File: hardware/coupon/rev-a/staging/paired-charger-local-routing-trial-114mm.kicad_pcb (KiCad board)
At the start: 6 copper layers, 114 x 32.5 mm, 483 parts, among them J1 USB4505-03-0-A, J2 S2B-PH-SM4-TB, SW1 EVQP7J01P, SW2 JS202011JCQN, U1 TLC59581RTQT, U11 SN74LVC1G04DBVR, U17 SN74LVC1G11DBVR, U2 74HC4514PW,118, U23 SN74LVC1G06DBVR, U24 SN74LVC2G17DBVR, U25 SN74LVC2G17DBVR, U29 TPS70933DBVR, U3 ESP32-S3-WROOM-1U-N16R8, U31 TUSB320LAIRWBR, U32 TS3USB31ERSER, U33 TPD4E05U06DQAR, U34 TPS3808G01DBVR, U35 MAX17048G+T10, U36 TPS631000DRLR, U37 TPS63020DSJT, U38 2.5V shunt, U39 TMP390A2DRLR, U40 SN74AUP1G125DBVR, U41 BQ24074RGTR, U42 SN74AUP1G125DBVR, U43 SN74AUP1G125DBVR, U44 TPS259474ARPWR, U45 TPS259474ARPWR, U46 TCA9517ADGKR, U47 TPS3823A-33DBVR, U48 SN74LVC1G04DSFR, U49 SN74LVC1G74RSER, U50 SN74LVC1G74RSER, U51 SN74LVC1G11DRYR, U52 SN74LVC1G08DSFR, U53 TLV6700DSER, U54 SN74LVC2G00DCUR, U55 SN74LVC2G08DCUR

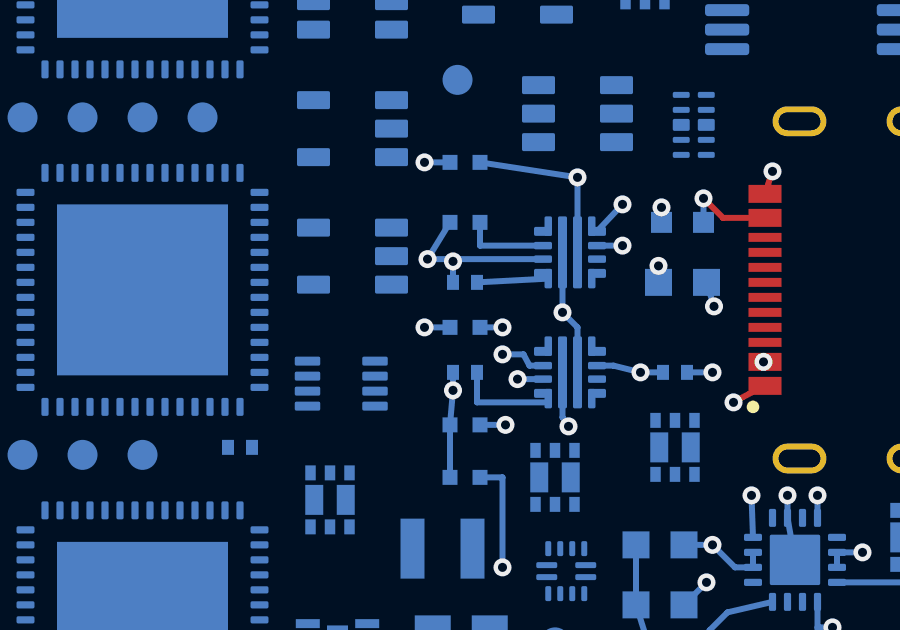
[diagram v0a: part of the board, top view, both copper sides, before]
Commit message: Route local charger permission to E1 enable
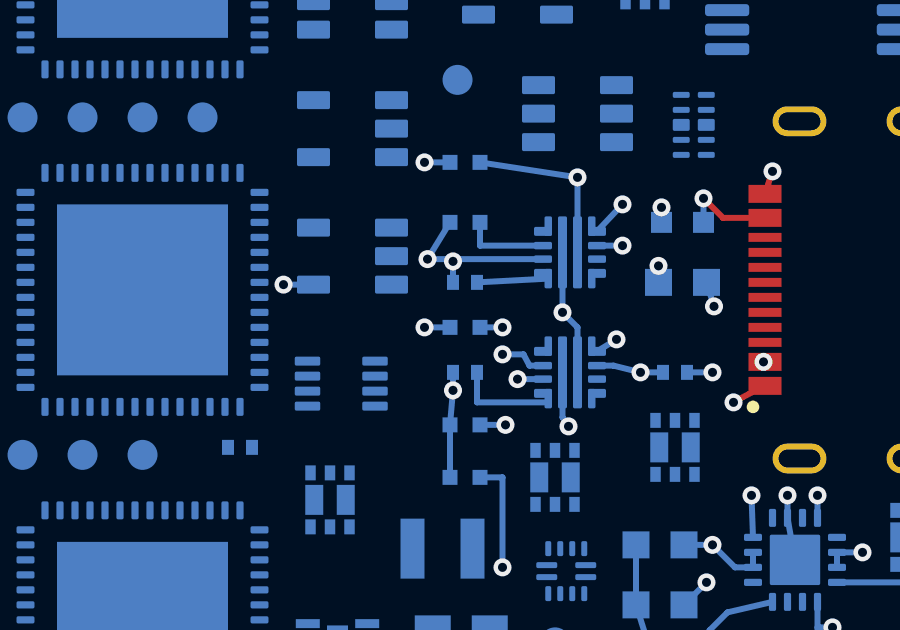
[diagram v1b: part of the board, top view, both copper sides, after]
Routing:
- net CHARGER_GATE_EN: track 0.00 -> 16.1 mm, vias 0 -> 2
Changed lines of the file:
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@@
+	)
+	(segment
+		(start 101 14.3)
+		(end 102.3 17.9)
+		(width 0.2)
+		(layer "In1.Cu")
+		(net "CHARGER_GATE_EN")
 	)
 	(segment
@@
 		(layer "B.Cu")
 		(net "GND")
+	)
+	(segment
+		(start 102.3 17.9)
+		(end 101.65 18.3)
+		(width 0.2)
+		(layer "B.Cu")
+		(net "CHARGER_GATE_EN")
 	)
 	(segment
@@
 	)
 	(segment
+		(start 91.2 16.075)
+		(end 93 14.3)
+		(width 0.2)
+		(layer "In1.Cu")
+		(net "CHARGER_GATE_EN")
+	)
+	(segment
+		(start 92.2 16.075)
+		(end 91.2 16.075)
+		(width 0.2)
+		(layer "B.Cu")
+		(net "CHARGER_GATE_EN")
+	)
+	(segment
+		(start 93 14.3)
+		(end 101 14.3)
+		(width 0.2)
+		(layer "In1.Cu")
+		(net "CHARGER_GATE_EN")
+	)
+	(segment
 		(start 95.9 12)
 		(end 100 11.5)
@@
 	)
 	(via
+		(at 102.3 17.9)
+		(size 0.6)
+		(drill 0.3)
+		(layers "F.Cu" "B.Cu")
+		(net "CHARGER_GATE_EN")
+	)
+	(via
 		(at 102.5 13.4)
 		(size 0.6)
@@
 	)
 	(via
+		(at 91.2 16.075)
+		(size 0.6)
+		(drill 0.3)
+		(layers "F.Cu" "B.Cu")
+		(net "CHARGER_GATE_EN")
+	)
+	(via

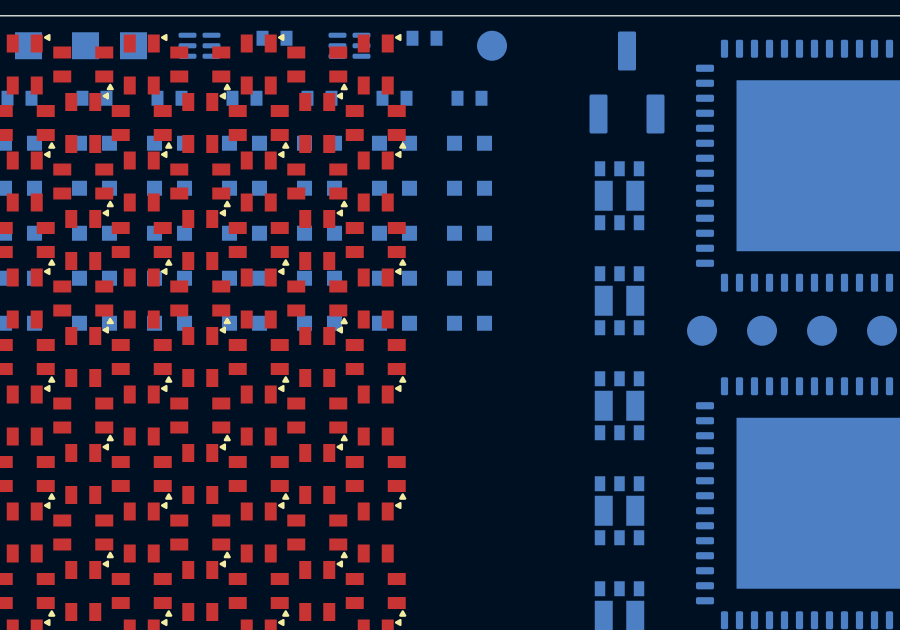
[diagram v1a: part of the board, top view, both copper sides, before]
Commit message: Connect E1 enable bias resistors on 114 mm trial
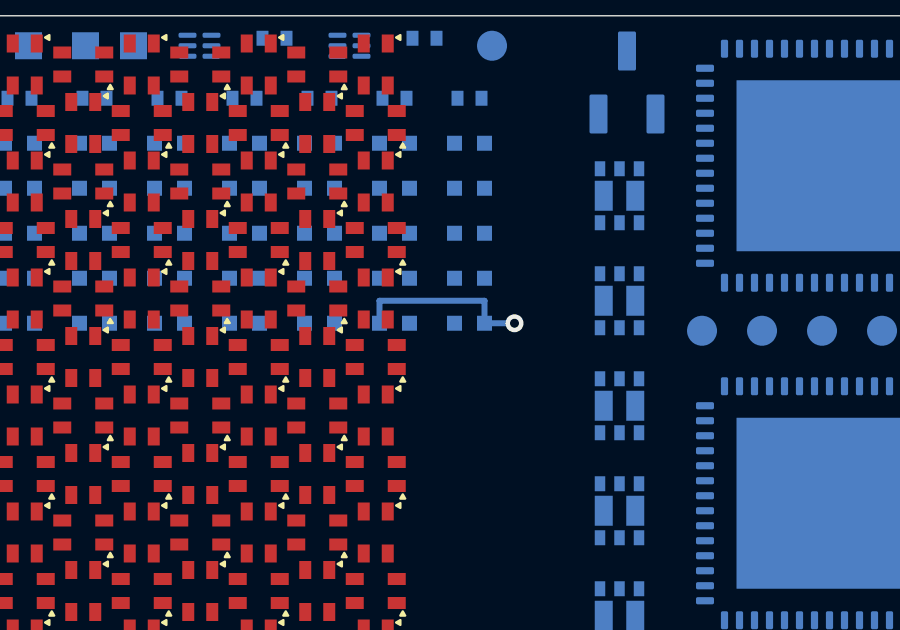
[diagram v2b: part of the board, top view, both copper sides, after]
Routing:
- net CHARGER_GATE_EN: track 16.1 -> 38.2 mm, vias 2 -> 3
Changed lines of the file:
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@@
+	)
+	(segment
+		(start 71.75 10.25)
+		(end 71.75 9.5)
+		(width 0.2)
+		(layer "B.Cu")
+		(net "CHARGER_GATE_EN")
+	)
+	(segment
+		(start 71.75 9.5)
+		(end 75.25 9.5)
+		(width 0.2)
+		(layer "B.Cu")
+		(net "CHARGER_GATE_EN")
+	)
+	(segment
+		(start 75.25 10.25)
+		(end 76.25 10.25)
+		(width 0.2)
+		(layer "B.Cu")
+		(net "CHARGER_GATE_EN")
+	)
+	(segment
+		(start 75.25 9.5)
+		(end 75.25 10.25)
+		(width 0.2)
+		(layer "B.Cu")
+		(net "CHARGER_GATE_EN")
+	)
+	(segment
+		(start 76.25 10.25)
+		(end 91.2 16.075)
+		(width 0.2)
+		(layer "In1.Cu")
+		(net "CHARGER_GATE_EN")
 	)
 	(segment
@@
 	)
 	(via
+		(at 76.25 10.25)
+		(size 0.6)
+		(drill 0.3)
+		(layers "F.Cu" "B.Cu")
+		(net "CHARGER_GATE_EN")
+	)
+	(via

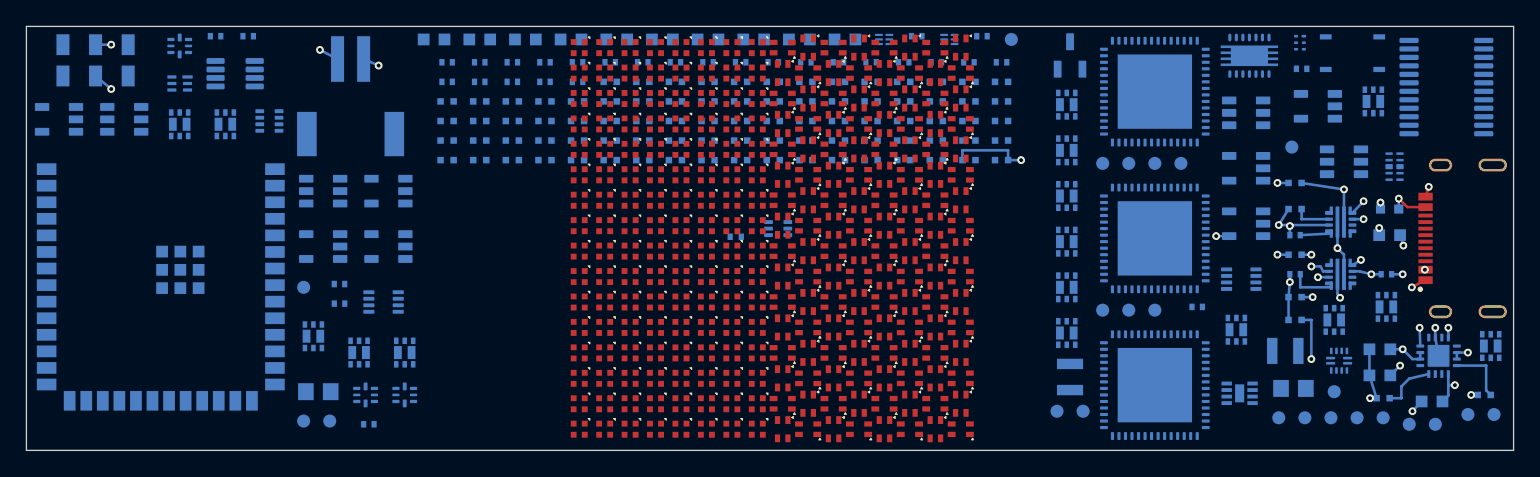
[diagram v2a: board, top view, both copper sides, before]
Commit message: Route charger inhibit node and local supervisor links on 114mm trial
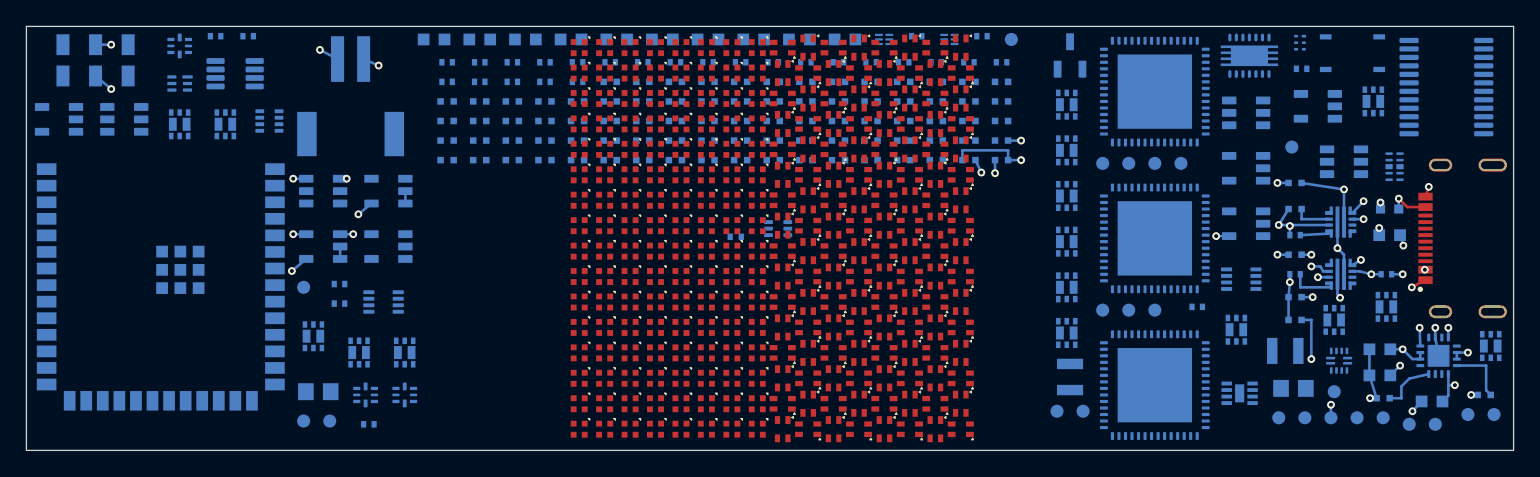
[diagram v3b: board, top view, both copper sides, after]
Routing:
- net CHARGER_GATE_EN: track 38.2 -> 126.6 mm, vias 3 -> 6
- net +3V3_USB: track 0.00 -> 12.2 mm, vias 0 -> 4
- net GND: track 182.1 -> 191.8 mm, vias 16 -> 17
- net USB_RAW_LOGIC_READY: track 0.00 -> 5.96 mm, vias 0 -> 2
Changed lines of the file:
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@@
+	)
+	(segment
+		(start 100 29)
+		(end 90 29)
+		(width 0.2)
+		(layer "In4.Cu")
+		(net "CHARGER_GATE_EN")
+	)
+	(segment
+		(start 100.001262 30.000001)
+		(end 100 29)
+		(width 0.2)
+		(layer "B.Cu")
+		(net "CHARGER_GATE_EN")
 	)
 	(segment
@@
 		(layer "B.Cu")
 		(net "CHARGER_ILIM")
+	)
+	(segment
+		(start 20.35 18.75)
+		(end 25.45 14.4)
+		(width 0.2)
+		(layer "In4.Cu")
+		(net "CHARGER_GATE_EN")
+	)
+	(segment
+		(start 20.45 11.675)
+		(end 20.45 15.925)
+		(width 0.2)
+		(layer "In2.Cu")
+		(net "+3V3_USB")
+	)
+	(segment
+		(start 21.45 11.675)
+		(end 20.45 11.675)
+		(width 0.2)
+		(layer "B.Cu")
+		(net "+3V3_USB")
+	)
+	(segment
+		(start 21.45 15.925)
+		(end 20.45 15.925)
+		(width 0.2)
+		(layer "B.Cu")
+		(net "+3V3_USB")
+	)
+	(segment
+		(start 21.45 17.825)
+		(end 20.35 18.75)
+		(width 0.2)
+		(layer "B.Cu")
+		(net "CHARGER_GATE_EN")
 	)
 	(segment
@@
 	)
 	(segment
+		(start 24.05 11.675)
+		(end 24.55 11.675)
+		(width 0.2)
+		(layer "B.Cu")
+		(net "USB_RAW_LOGIC_READY")
+	)
+	(segment
+		(start 24.05 15.925)
+		(end 25.05 15.925)
+		(width 0.2)
+		(layer "B.Cu")
+		(net "USB_RAW_LOGIC_READY")
+	)
+	(segment
+		(start 24.05 16.875)
+		(end 24.05 17.825)
+		(width 0.2)
+		(layer "B.Cu")
+		(net "GND")
+	)
+	(segment
+		(start 24.55 11.675)
+		(end 24.55 15.425)
+		(width 0.2)
+		(layer "In2.Cu")
+		(net "USB_RAW_LOGIC_READY")
+	)
+	(segment
+		(start 24.55 15.425)
+		(end 25.05 15.925)
+		(width 0.2)
+		(layer "In2.Cu")
+		(net "USB_RAW_LOGIC_READY")
+	)
+	(segment
+		(start 25.45 14.4)
+		(end 30 14.4)
+		(width 0.2)
+		(layer "In4.Cu")
+		(net "CHARGER_GATE_EN")
+	)
+	(segment
 		(start 25.85 2.5)
 		(end 27 3)
@@
 		(layer "B.Cu")
 		(net "+BAT_PROTECTED_DRAFT")
+	)
+	(segment
+		(start 26.45 13.575)
+		(end 25.45 14.4)
+		(width 0.2)
+		(layer "B.Cu")
+		(net "CHARGER_GATE_EN")
 	)
 	(segment
@@
 	)
 	(segment
+		(start 29.05 12.625)
+		(end 29.05 13.575)
+		(width 0.2)
+		(layer "B.Cu")
+		(net "GND")
+	)
+	(segment
 		(start 30 1.8)
 		(end 103 28.5)
@@
 		(layer "In2.Cu")
 		(net "GND")
+	)
+	(segment
+		(start 30 14.4)
+		(end 75 14.4)
+		(width 0.2)
+		(layer "In4.Cu")
+		(net "CHARGER_GATE_EN")
 	)
 	(segment
@@
 	)
 	(segment
+		(start 72.75 10.25)
+		(end 73.2 11.2)
+		(width 0.2)
+		(layer "B.Cu")
+		(net "+3V3_USB")
+	)
+	(segment
+		(start 73.2 11.2)
+		(end 76.25 8.75)
+		(width 0.2)
+		(layer "In2.Cu")
+		(net "+3V3_USB")
+	)
+	(segment
+		(start 74.25 10.25)
+		(end 74.25 11.25)
+		(width 0.2)
+		(layer "B.Cu")
+		(net "GND")
+	)
+	(segment
+		(start 74.25 11.25)
+		(end 74.25 18)
+		(width 0.2)
+		(layer "In2.Cu")
+		(net "GND")
+	)
+	(segment
+		(start 75 14.4)
+		(end 76.25 10.25)
+		(width 0.2)
+		(layer "In4.Cu")
+		(net "CHARGER_GATE_EN")
+	)
+	(segment
 		(start 75.25 10.25)
 		(end 76.25 10.25)
@@
 	)
 	(segment
+		(start 75.25 8.75)
+		(end 76.25 8.75)
+		(width 0.2)
+		(layer "B.Cu")
+		(net "+3V3_USB")
+	)
+	(segment
 		(start 75.25 9.5)
 		(end 75.25 10.25)
@@
 	)
 	(segment
+		(start 90 16.075)
+		(end 91.2 16.075)
+		(width 0.2)
+		(layer "In4.Cu")
+		(net "CHARGER_GATE_EN")
+	)
+	(segment
+		(start 90 29)
+		(end 90 16.075)
+		(width 0.2)
+		(layer "In4.Cu")
+		(net "CHARGER_GATE_EN")
+	)
+	(segment
 		(start 91.2 16.075)
 		(end 93 14.3)
@@
 	)
 	(via
+		(at 100 29)
+		(size 0.6)
+		(drill 0.3)
+		(layers "F.Cu" "B.Cu")
+		(net "CHARGER_GATE_EN")
+	)
+	(via
 		(at 100.5 17)
 		(size 0.6)
@@
 	)
 	(via
+		(at 20.35 18.75)
+		(size 0.6)
+		(drill 0.3)
+		(layers "F.Cu" "B.Cu")
+		(net "CHARGER_GATE_EN")
+	)
+	(via
+		(at 20.45 11.675)
+		(size 0.6)
+		(drill 0.3)
+		(layers "F.Cu" "B.Cu")
+		(net "+3V3_USB")
+	)
+	(via
+		(at 20.45 15.925)
+		(size 0.6)
+		(drill 0.3)
+		(layers "F.Cu" "B.Cu")
+		(net "+3V3_USB")
+	)
+	(via
 		(at 22.5 1.8)
 		(size 0.6)
@@
 	)
 	(via
+		(at 24.55 11.675)
+		(size 0.6)
+		(drill 0.3)
+		(layers "F.Cu" "B.Cu")
+		(net "USB_RAW_LOGIC_READY")
+	)
+	(via
+		(at 25.05 15.925)
+		(size 0.6)
+		(drill 0.3)
+		(layers "F.Cu" "B.Cu")
+		(net "USB_RAW_LOGIC_READY")
+	)
+	(via
+		(at 25.45 14.4)
+		(size 0.6)
+		(drill 0.3)
+		(layers "F.Cu" "B.Cu")
+		(net "CHARGER_GATE_EN")
+	)
+	(via
 		(at 27 3)
 		(size 0.6)
@@
 	)
 	(via
+		(at 73.2 11.2)
+		(size 0.6)
+		(drill 0.3)
+		(layers "F.Cu" "B.Cu")
+		(net "+3V3_USB")
+	)
+	(via
+		(at 74.25 11.25)
+		(size 0.6)
+		(drill 0.3)
+		(layers "F.Cu" "B.Cu")
+		(net "GND")
+	)
+	(via
 		(at 76.25 10.25)
 		(size 0.6)
@@
 	)
 	(via
+		(at 76.25 8.75)
+		(size 0.6)
+		(drill 0.3)
+		(layers "F.Cu" "B.Cu")
+		(net "+3V3_USB")
+	)
+	(via

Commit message: Route source charge request and local logic returns
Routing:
- net GND: track 191.8 -> 206.9 mm, vias 17 -> 18
- net +3V3_USB: track 12.2 -> 24.2 mm, vias 4 -> 6
- net USB_CHARGE_REQ: track 0.00 -> 9.69 mm, vias 0 -> 2
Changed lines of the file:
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@@
+	)
+	(segment
+		(start 90 14.175)
+		(end 91.2 14.175)
+		(width 0.2)
+		(layer "In2.Cu")
+		(net "+3V3_USB")
 	)
 	(segment
@@
 	)
 	(segment
+		(start 90 6.625)
+		(end 90 14.175)
+		(width 0.2)
+		(layer "In2.Cu")
+		(net "+3V3_USB")
+	)
+	(segment
 		(start 91.2 16.075)
 		(end 93 14.3)
@@
 	)
 	(segment
+		(start 91.2 6.625)
+		(end 90 6.625)
+		(width 0.2)
+		(layer "In2.Cu")
+		(net "+3V3_USB")
+	)
+	(segment
+		(start 91.3 7.575)
+		(end 93.5 9.775)
+		(width 0.2)
+		(layer "In4.Cu")
+		(net "USB_CHARGE_REQ")
+	)
+	(segment
+		(start 92.2 14.175)
+		(end 91.2 14.175)
+		(width 0.2)
+		(layer "B.Cu")
+		(net "+3V3_USB")
+	)
+	(segment
 		(start 92.2 16.075)
 		(end 91.2 16.075)
@@
 	)
 	(segment
+		(start 92.2 6.625)
+		(end 91.2 6.625)
+		(width 0.2)
+		(layer "B.Cu")
+		(net "+3V3_USB")
+	)
+	(segment
+		(start 92.2 7.575)
+		(end 91.3 7.575)
+		(width 0.2)
+		(layer "B.Cu")
+		(net "USB_CHARGE_REQ")
+	)
+	(segment
 		(start 93 14.3)
 		(end 101 14.3)
@@
 	)
 	(segment
+		(start 93.5 13.175)
+		(end 94.8 13.2)
+		(width 0.2)
+		(layer "In4.Cu")
+		(net "USB_CHARGE_REQ")
+	)
+	(segment
+		(start 93.5 9.775)
+		(end 93.5 13.175)
+		(width 0.2)
+		(layer "In4.Cu")
+		(net "USB_CHARGE_REQ")
+	)
+	(segment
+		(start 94 14.7)
+		(end 96 15.22)
+		(width 0.2)
+		(layer "In2.Cu")
+		(net "GND")
+	)
+	(segment
+		(start 94 6.625)
+		(end 94 14.7)
+		(width 0.2)
+		(layer "In2.Cu")
+		(net "GND")
+	)
+	(segment
+		(start 94.8 14.175)
+		(end 94.8 13.2)
+		(width 0.2)
+		(layer "B.Cu")
+		(net "USB_CHARGE_REQ")
+	)
+	(segment
+		(start 94.8 15.125)
+		(end 94.8 16.075)
+		(width 0.2)
+		(layer "B.Cu")
+		(net "GND")
+	)
+	(segment
+		(start 94.8 15.125)
+		(end 96 15.22)
+		(width 0.2)
+		(layer "B.Cu")
+		(net "GND")
+	)
+	(segment
+		(start 94.8 6.625)
+		(end 95.8 6.625)
+		(width 0.2)
+		(layer "B.Cu")
+		(net "GND")
+	)
+	(segment
+		(start 95.8 6.625)
+		(end 94 6.625)
+		(width 0.2)
+		(layer "In2.Cu")
+		(net "GND")
+	)
+	(segment
 		(start 95.9 12)
 		(end 100 11.5)
@@
 	)
 	(via
+		(at 91.2 14.175)
+		(size 0.6)
+		(drill 0.3)
+		(layers "F.Cu" "B.Cu")
+		(net "+3V3_USB")
+	)
+	(via
 		(at 91.2 16.075)
 		(size 0.6)
@@
 	)
 	(via
+		(at 91.2 6.625)
+		(size 0.6)
+		(drill 0.3)
+		(layers "F.Cu" "B.Cu")
+		(net "+3V3_USB")
+	)
+	(via
+		(at 91.3 7.575)
+		(size 0.6)
+		(drill 0.3)
+		(layers "F.Cu" "B.Cu")
+		(net "USB_CHARGE_REQ")
+	)
+	(via
+		(at 94.8 13.2)
+		(size 0.6)
+		(drill 0.3)
+		(layers "F.Cu" "B.Cu")
+		(net "USB_CHARGE_REQ")
+	)
+	(via
+		(at 95.8 6.625)
+		(size 0.6)
+		(drill 0.3)
+		(layers "F.Cu" "B.Cu")
+		(net "GND")
+	)
+	(via

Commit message: Route temperature inhibit and remaining sink grounds
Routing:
- net TEMP_OK: track 0.00 -> 82.3 mm, vias 0 -> 2
- net GND: track 206.9 -> 229.2 mm, vias 18 -> 20
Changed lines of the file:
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@@
+	)
+	(segment
+		(start 24.05 17.825)
+		(end 25 18.5)
+		(width 0.2)
+		(layer "B.Cu")
+		(net "GND")
 	)
 	(segment
@@
 		(layer "In2.Cu")
 		(net "USB_RAW_LOGIC_READY")
+	)
+	(segment
+		(start 25 18.5)
+		(end 31 13.575)
+		(width 0.2)
+		(layer "In2.Cu")
+		(net "GND")
 	)
 	(segment
@@
 	)
 	(segment
+		(start 29.05 11.675)
+		(end 29.9 11.675)
+		(width 0.2)
+		(layer "B.Cu")
+		(net "TEMP_OK")
+	)
+	(segment
 		(start 29.05 12.625)
 		(end 29.05 13.575)
@@
 		(layer "B.Cu")
 		(net "GND")
+	)
+	(segment
+		(start 29.05 13.575)
+		(end 31 13.575)
+		(width 0.2)
+		(layer "B.Cu")
+		(net "GND")
+	)
+	(segment
+		(start 29.9 11.675)
+		(end 30 9.5)
+		(width 0.2)
+		(layer "In4.Cu")
+		(net "TEMP_OK")
 	)
 	(segment
@@
 	)
 	(segment
+		(start 30 9.5)
+		(end 77.5 9.5)
+		(width 0.2)
+		(layer "In4.Cu")
+		(net "TEMP_OK")
+	)
+	(segment
+		(start 31 13.575)
+		(end 31 2.166)
+		(width 0.2)
+		(layer "In2.Cu")
+		(net "GND")
+	)
+	(segment
 		(start 5.3 1.4)
 		(end 6.5 1.4)
@@
 		(layer "B.Cu")
 		(net "+BAT_PROTECTED_DRAFT")
+	)
+	(segment
+		(start 56 13.5)
+		(end 67.5 13.5)
+		(width 0.2)
+		(layer "B.Cu")
+		(net "TEMP_OK")
+	)
+	(segment
+		(start 56 15)
+		(end 56 13.5)
+		(width 0.2)
+		(layer "B.Cu")
+		(net "TEMP_OK")
+	)
+	(segment
+		(start 56 15)
+		(end 56 16)
+		(width 0.2)
+		(layer "B.Cu")
+		(net "TEMP_OK")
+	)
+	(segment
+		(start 56 16)
+		(end 56.885 16)
+		(width 0.2)
+		(layer "B.Cu")
+		(net "TEMP_OK")
+	)
+	(segment
+		(start 56.885 15)
+		(end 56 15)
+		(width 0.2)
+		(layer "B.Cu")
+		(net "TEMP_OK")
 	)
 	(segment
@@
 	)
 	(segment
+		(start 67.5 13.5)
+		(end 69.25 11.75)
+		(width 0.2)
+		(layer "B.Cu")
+		(net "TEMP_OK")
+	)
+	(segment
+		(start 69.25 11.75)
+		(end 69.25 10.25)
+		(width 0.2)
+		(layer "B.Cu")
+		(net "TEMP_OK")
+	)
+	(segment
+		(start 69.25 11.75)
+		(end 69.25 12.1)
+		(width 0.2)
+		(layer "B.Cu")
+		(net "TEMP_OK")
+	)
+	(segment
+		(start 69.25 12.1)
+		(end 77.5 12.1)
+		(width 0.2)
+		(layer "B.Cu")
+		(net "TEMP_OK")
+	)
+	(segment
 		(start 71.75 10.25)
 		(end 71.75 9.5)
@@
 	)
 	(segment
+		(start 77.5 12.1)
+		(end 77.5 12.5)
+		(width 0.2)
+		(layer "B.Cu")
+		(net "TEMP_OK")
+	)
+	(segment
+		(start 77.5 9.5)
+		(end 77.5 12.5)
+		(width 0.2)
+		(layer "In4.Cu")
+		(net "TEMP_OK")
+	)
+	(segment
 		(start 90 14.175)
 		(end 91.2 14.175)
@@
 	)
 	(via
+		(at 25 18.5)
+		(size 0.6)
+		(drill 0.3)
+		(layers "F.Cu" "B.Cu")
+		(net "GND")
+	)
+	(via
 		(at 25.05 15.925)
 		(size 0.6)
@@
 	)
 	(via
+		(at 29.9 11.675)
+		(size 0.6)
+		(drill 0.3)
+		(layers "F.Cu" "B.Cu")
+		(net "TEMP_OK")
+	)
+	(via
+		(at 31 13.575)
+		(size 0.6)
+		(drill 0.3)
+		(layers "F.Cu" "B.Cu")
+		(net "GND")
+	)
+	(via
 		(at 6.5 1.4)
 		(size 0.6)
@@
 	)
 	(via
+		(at 77.5 12.5)
+		(size 0.6)
+		(drill 0.3)
+		(layers "F.Cu" "B.Cu")
+		(net "TEMP_OK")
+	)
+	(via
